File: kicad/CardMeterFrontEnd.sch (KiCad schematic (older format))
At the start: 24 parts, among them J1 V+, J2 R-, J3 A+, J4 COM, J5 Analog, J6 Gain, J7 ADC, U1 LTC1992, U2 AD8231, U3 LTC2315

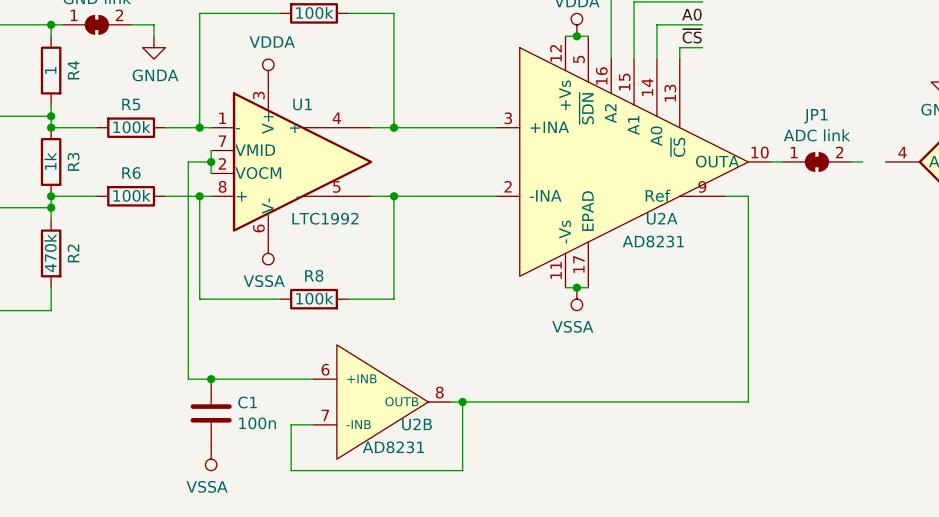
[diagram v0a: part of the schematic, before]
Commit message: front and is working
Common Mode problem, probably due to resistor matching
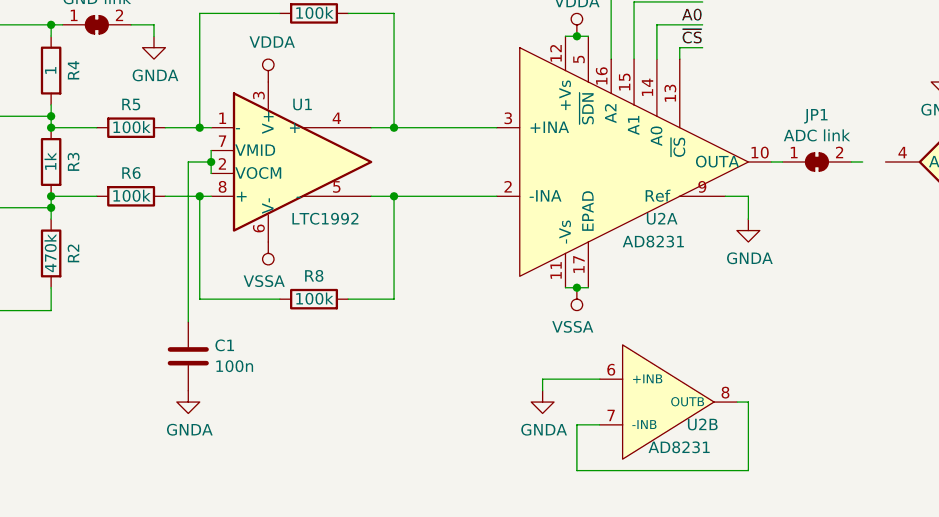
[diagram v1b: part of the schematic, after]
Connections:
- net GNDA: now also C1.2, U2.6 (+INB), U2.9 (Ref)
- net VSSA: no longer C1.2
- net at C1.1, U1.2 (VOCM), U1.7 (VMID): no longer U2.6 (+INB)
- net at U2.7 (-INB), U2.8 (OUTB): no longer U2.9 (Ref)
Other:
- moved on the sheet: C1, U2B
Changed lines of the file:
@@
 EESchema Schematic File Version 4
+LIBS:CardMeterFrontEnd-cache
 EELAYER 30 0
 EELAYER END
@@
 L telec:AD8231 U2
 U 2 1 5DC87137
-P 3500 3700
-F 0 "U2" H 3850 3600 50  0000 C CNN
-F 1 "AD8231" H 3750 3500 50  0000 C CNN
-F 2 "Package_CSP:LFCSP-16-1EP_4x4mm_P0.65mm_EP2.1x2.1mm" H 3650 3050 50  0001 C CNN
-F 3 "" H 4100 3900 50  0001 C CNN
-	2    3500 3700
+P 4750 3700
+F 0 "U2" H 5100 3600 50  0000 C CNN
+F 1 "AD8231" H 5000 3500 50  0000 C CNN
+F 2 "Package_CSP:LFCSP-16-1EP_4x4mm_P0.65mm_EP2.1x2.1mm" H 4900 3050 50  0001 C CNN
+F 3 "" H 5350 3900 50  0001 C CNN
+	2    4750 3700
 	1    0    0    -1
 $EndComp
@@
 L Device:C C1
 U 1 1 5DC90D61
-P 2950 3750
-F 0 "C1" H 3065 3796 50  0000 L CNN
-F 1 "100n" H 3065 3705 50  0000 L CNN
-F 2 "Capacitor_SMD:C_0805_2012Metric_Pad1.15x1.40mm_HandSolder" H 2988 3600 50  0001 C CNN
-F 3 "~" H 2950 3750 50  0001 C CNN
-	1    2950 3750
-	1    0    0    -1
-$EndComp
-Wire Wire Line
-	3400 3800 3300 3800
-Wire Wire Line
-	3300 3800 3300 4000
-Wire Wire Line
-	3300 4000 4050 4000
-Wire Wire Line
-	4050 4000 4050 3700
-Wire Wire Line
-	4050 3700 4000 3700
+P 2850 3500
+F 0 "C1" H 2965 3546 50  0000 L CNN
+F 1 "100n" H 2965 3455 50  0000 L CNN
+F 2 "Capacitor_SMD:C_0805_2012Metric_Pad1.15x1.40mm_HandSolder" H 2888 3350 50  0001 C CNN
+F 3 "~" H 2850 3500 50  0001 C CNN
+	1    2850 3500
+	1    0    0    -1
+$EndComp
+Wire Wire Line
+	4650 3800 4550 3800
+Wire Wire Line
+	4550 3800 4550 4000
+Wire Wire Line
+	4550 4000 5300 4000
+Wire Wire Line
+	5300 4000 5300 3700
+Wire Wire Line
+	5300 3700 5250 3700
 Wire Wire Line
 	4500 3200 4550 3200
@@
 	5400 2650 5450 2650
 Wire Wire Line
-	4050 3700 5300 3700
-Wire Wire Line
-	5300 3700 5300 2800
+	5300 2900 5300 2800
 Wire Wire Line
 	5300 2800 5200 2800
-Connection ~ 4050 3700
 Wire Wire Line
 	4500 2100 4550 2100
@@
 	4550 2100 4600 2100
 Wire Wire Line
-	3400 3600 2950 3600
-Wire Wire Line
-	2850 3600 2850 2650
+	4650 3600 4400 3600
 Wire Wire Line
 	2850 2650 2950 2650
@@
 	2950 2650 2950 2600
 Connection ~ 2950 2650
-Connection ~ 2950 3600
-Wire Wire Line
-	2950 3600 2850 3600
 $Comp
 L Device:R R5
@@
 	1    7750 1750
 	1    0    0    -1
-$EndComp
-$Comp
-L power:VSSA #PWR0102
-U 1 1 5DDDF5F4
-P 2950 3900
-F 0 "#PWR0102" H 2950 3750 50  0001 C CNN
-F 1 "VSSA" H 2968 4073 50  0000 C CNN
-F 2 "" H 2950 3900 50  0001 C CNN
-F 3 "" H 2950 3900 50  0001 C CNN
-	1    2950 3900
-	-1   0    0    1
 $EndComp
 Text Label 7350 2650 0    50   ~ 0
@@
 Text Label 7350 1950 0    50   ~ 0
 ~CS
+Wire Wire Line
+	2850 3350 2850 2650
+$Comp
+L power:GNDA #PWR?
+U 1 1 5E2A4A37
+P 2850 3650
+F 0 "#PWR?" H 2850 3400 50  0001 C CNN
+F 1 "GNDA" H 2855 3477 50  0000 C CNN
+F 2 "" H 2850 3650 50  0001 C CNN
+F 3 "" H 2850 3650 50  0001 C CNN
+	1    2850 3650
+	1    0    0    -1
+$EndComp
+$Comp
+L power:GNDA #PWR?
+U 1 1 5E2A50E0
+P 4400 3650
+F 0 "#PWR?" H 4400 3400 50  0001 C CNN
+F 1 "GNDA" H 4405 3477 50  0000 C CNN
+F 2 "" H 4400 3650 50  0001 C CNN
+F 3 "" H 4400 3650 50  0001 C CNN
+	1    4400 3650
+	1    0    0    -1
+$EndComp
+$Comp
+L power:GNDA #PWR?
+U 1 1 5E2A57E0
+P 5300 2900
+F 0 "#PWR?" H 5300 2650 50  0001 C CNN
+F 1 "GNDA" H 5305 2727 50  0000 C CNN
+F 2 "" H 5300 2900 50  0001 C CNN
+F 3 "" H 5300 2900 50  0001 C CNN
+	1    5300 2900
+	1    0    0    -1
+$EndComp
+Wire Wire Line
+	4400 3650 4400 3600
 $EndSCHEMATC
